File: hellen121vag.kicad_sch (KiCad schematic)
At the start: 122 parts, among them J1 USB_B_Mini, J10 AudioJack_THR, J2 Conn_01x01, J3 Conn_01x01, J4 Conn_01x01, J5 Conn_01x01, J6 Conn_01x01, J7 Conn_01x08, J8 Conn_01x06, M1 Module-can-0.1, M10 Module-can-0.1, M11 Module-vr-0.1, M12 Module-dinput4-0.1, M2 Module-power5-0.2, M3 Module-mcu-0.2, M4 Module-input-0.1, M5 Module-knock-0.1, M6 Module-output-0.2, M7 Module-ign8-0.1, M8 Module-power12-0.2, M9 Module-wbo-0.1, P1 368255-2, P10 Pad, P11 Pad, P12 Pad, P13 Pad, P14 Pad, P17 Pad, P2 Pad, P20 Pad, P28 Pad, P3 Pad, P4 Pad, P40 Pad, P41 Pad, P43 Pad, P44 Pad, P45 Pad, P46 Pad, P48 Pad, P49 Pad, P5 Pad, P56 Pad, P6 Pad, P61 Pad, P63 Pad, P64 Pad, P66 Pad, P67 Pad, P68 Pad, P69 Pad, P7 Pad, P74 Pad, P8 Pad, P80 Pad, P9 Pad, U1 L6205PD, U2 LPS25HB, U3 MCP6002-xSN

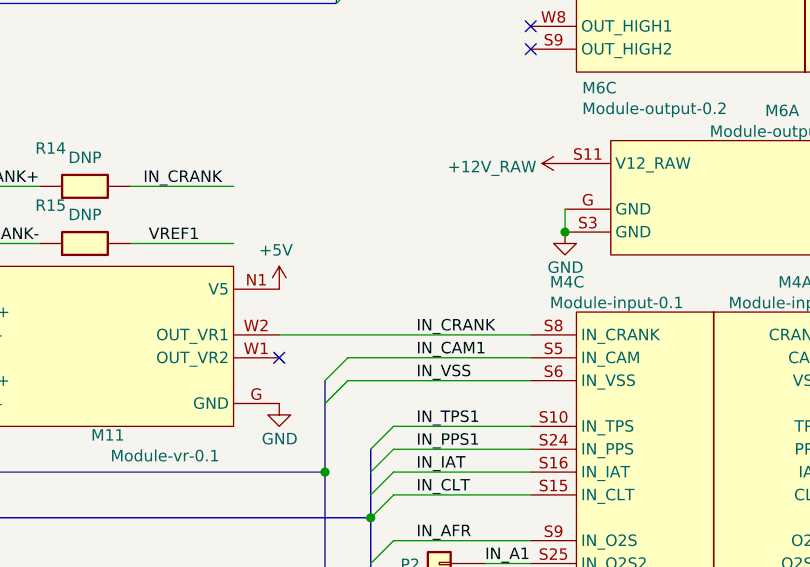
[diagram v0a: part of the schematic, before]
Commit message: Implement & Document trigger HW solder hookup pins #48
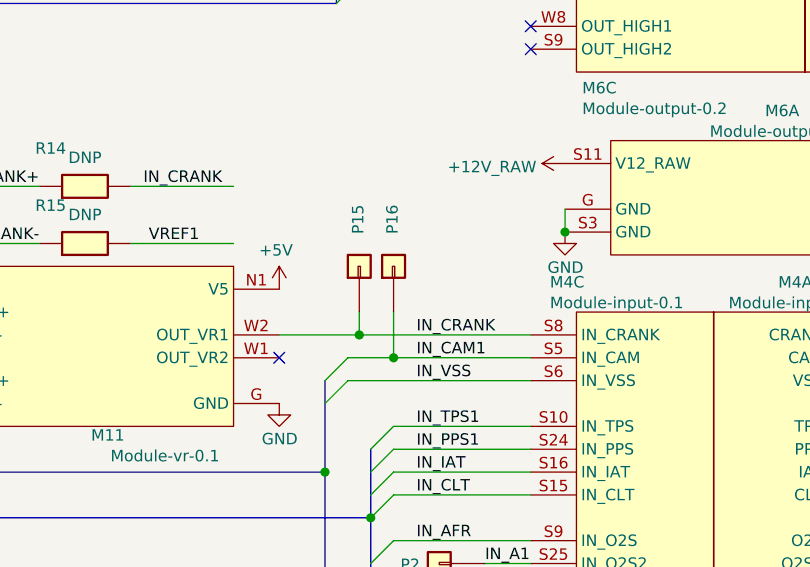
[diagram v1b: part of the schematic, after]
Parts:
- added P15, P16: Pad, hellen-one-common:PAD-TH, symbol hellen-one-common:Pad
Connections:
- net IN_CAM1: now also P16.1 (Pin_1)
- net IN_CRANK: now also P15.1 (Pin_1)
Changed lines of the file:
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@@
-(kicad_sch (version 20210406) (generator eeschema)
+(kicad_sch (version 20210621) (generator eeschema)
   (paper "A2")
   (title_block
@@
   (junction (at 280.67 134.62) (diameter 1.016) (color 0 0 0 0))
   (junction (at 284.48 346.71) (diameter 1.016) (color 0 0 0 0))
+  (junction (at 285.75 196.85) (diameter 1.016) (color 0 0 0 0))
   (junction (at 287.02 119.38) (diameter 1.016) (color 0 0 0 0))
   (junction (at 287.02 121.92) (diameter 1.016) (color 0 0 0 0))
   (junction (at 287.02 273.05) (diameter 1.016) (color 0 0 0 0))
+  (junction (at 289.56 199.39) (diameter 1.016) (color 0 0 0 0))
   (junction (at 294.64 346.71) (diameter 1.016) (color 0 0 0 0))
   (junction (at 302.26 152.4) (diameter 1.016) (color 0 0 0 0))
@@
     (stroke (width 0) (type solid) (color 0 0 0 0))
   )
-  (wire (pts (xy 276.86 196.85) (xy 304.8 196.85))
+  (wire (pts (xy 276.86 196.85) (xy 285.75 196.85))
     (stroke (width 0) (type solid) (color 0 0 0 0))
   )
@@
     (stroke (width 0) (type solid) (color 0 0 0 0))
   )
-  (wire (pts (xy 284.48 199.39) (xy 304.8 199.39))
+  (wire (pts (xy 284.48 199.39) (xy 289.56 199.39))
     (stroke (width 0) (type solid) (color 0 0 0 0))
   )
@@
     (stroke (width 0) (type solid) (color 0 0 0 0))
   )
+  (wire (pts (xy 285.75 194.31) (xy 285.75 196.85))
+    (stroke (width 0) (type solid) (color 0 0 0 0))
+  )
+  (wire (pts (xy 285.75 196.85) (xy 304.8 196.85))
+    (stroke (width 0) (type solid) (color 0 0 0 0))
+  )
   (wire (pts (xy 287.02 119.38) (xy 285.75 119.38))
     (stroke (width 0) (type solid) (color 0 0 0 0))
@@
     (stroke (width 0) (type solid) (color 0 0 0 0))
   )
+  (wire (pts (xy 289.56 194.31) (xy 289.56 199.39))
+    (stroke (width 0) (type solid) (color 0 0 0 0))
+  )
+  (wire (pts (xy 289.56 199.39) (xy 304.8 199.39))
+    (stroke (width 0) (type solid) (color 0 0 0 0))
+  )
   (wire (pts (xy 289.56 207.01) (xy 304.8 207.01))
     (stroke (width 0) (type solid) (color 0 0 0 0))
@@
     (pin "1")
   )
+  (symbol (lib_id "hellen-one-common:Pad") (at 285.75 189.23 90) (unit 1)
+    (in_bom yes) (on_board yes)
+    (property "Reference" "P15" (id 0) (at 285.6144 182.372 0)
+      (effects (font (size 1.27 1.27)) (justify right))
+    )
+    (property "Value" "Pad" (id 1) (at 288.29 189.23 0)
+      (effects (font (size 1.27 1.27)) hide)
+    )
+    (property "Footprint" "hellen-one-common:PAD-TH" (id 2) (at 289.56 189.23 0)
+      (effects (font (size 1.27 1.27)) hide)
+    )
+    (property "Datasheet" "~" (id 3) (at 285.75 189.23 0)
+      (effects (font (size 1.27 1.27)) hide)
+    )
+    (pin "1")
+  )
+  (symbol (lib_id "hellen-one-common:Pad") (at 289.56 189.23 90) (unit 1)
+    (in_bom yes) (on_board yes)
+    (property "Reference" "P16" (id 0) (at 289.4244 182.372 0)
+      (effects (font (size 1.27 1.27)) (justify right))
+    )
+    (property "Value" "Pad" (id 1) (at 292.1 189.23 0)
+      (effects (font (size 1.27 1.27)) hide)
+    )
+    (property "Footprint" "hellen-one-common:PAD-TH" (id 2) (at 293.37 189.23 0)
+      (effects (font (size 1.27 1.27)) hide)
+    )
+    (property "Datasheet" "~" (id 3) (at 289.56 189.23 0)
+      (effects (font (size 1.27 1.27)) hide)
+    )
+    (pin "1")
+  )
   (symbol (lib_id "hellen-one-common:Pad") (at 294.64 222.25 180) (unit 1)
     (in_bom yes) (on_board yes)
@@
       (reference "P14") (unit 1) (value "Pad") (footprint "hellen-one-common:PAD-TH")
     )
+    (path "/631638c1-bba7-416f-b9e2-d63828d88980"
+      (reference "P15") (unit 1) (value "Pad") (footprint "hellen-one-common:PAD-TH")
+    )
+    (path "/6af4d44c-79f6-417d-8cda-630cb6030fe1"
+      (reference "P16") (unit 1) (value "Pad") (footprint "hellen-one-common:PAD-TH")
+    )
     (path "/8149bcf9-72dd-4a61-a70c-152267751b88"

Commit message: less crazy routing for ignition outputs fix #32 Better match injector traces fix #45 Convert to 4 layer fix #56 Connect J1-6 USB cable shield to GND fix #62
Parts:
- added R23: 0, hellen-one-common:R0603, symbol hellen-one-common:Res
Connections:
- net GND: now also R23.2; no longer J1.5 (GND)
- net at J1.6 (Shield): now also J1.5 (GND), R23.1
- no-connect marks 67 -> 66
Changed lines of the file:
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@@
   (junction (at 398.78 382.27) (diameter 1.016) (color 0 0 0 0))
   (junction (at 398.78 397.51) (diameter 1.016) (color 0 0 0 0))
+  (junction (at 478.79 142.24) (diameter 1.016) (color 0 0 0 0))
   (junction (at 505.46 175.26) (diameter 1.016) (color 0 0 0 0))
   (junction (at 511.81 314.96) (diameter 1.016) (color 0 0 0 0))
@@
   (no_connect (at 441.96 170.18))
   (no_connect (at 468.63 149.86))
-  (no_connect (at 478.79 144.78))
   (no_connect (at 535.94 149.86))
   (bus_entry (at 95.25 80.01) (size 2.54 2.54)
@@
     (stroke (width 0) (type solid) (color 0 0 0 0))
   )
+  (wire (pts (xy 476.25 142.24) (xy 476.25 144.78))
+    (stroke (width 0) (type solid) (color 0 0 0 0))
+  )
+  (wire (pts (xy 478.79 142.24) (xy 476.25 142.24))
+    (stroke (width 0) (type solid) (color 0 0 0 0))
+  )
+  (wire (pts (xy 478.79 142.24) (xy 478.79 144.78))
+    (stroke (width 0) (type solid) (color 0 0 0 0))
+  )
   (wire (pts (xy 481.33 193.04) (xy 494.03 193.04))
     (stroke (width 0) (type solid) (color 0 0 0 0))
@@
     (stroke (width 0) (type solid) (color 0 0 0 0))
   )
+  (wire (pts (xy 485.14 142.24) (xy 478.79 142.24))
+    (stroke (width 0) (type solid) (color 0 0 0 0))
+  )
+  (wire (pts (xy 485.14 147.32) (xy 485.14 142.24))
+    (stroke (width 0) (type solid) (color 0 0 0 0))
+  )
   (wire (pts (xy 488.95 205.74) (xy 481.33 205.74))
     (stroke (width 0) (type solid) (color 0 0 0 0))
@@
     (pin "1")
   )
-  (symbol (lib_id "power:GND") (at 476.25 144.78 180) (unit 1)
+  (symbol (lib_id "power:GND") (at 485.14 157.48 0) (unit 1)
     (in_bom yes) (on_board yes)
-    (property "Reference" "#PWR0174" (id 0) (at 476.25 138.43 0)
+    (property "Reference" "#PWR0174" (id 0) (at 485.14 163.83 0)
       (effects (font (size 1.27 1.27)) hide)
     )
-    (property "Value" "GND" (id 1) (at 476.1992 140.8366 0))
-    (property "Footprint" "" (id 2) (at 476.25 144.78 0)
+    (property "Value" "GND" (id 1) (at 485.1908 161.4234 0))
+    (property "Footprint" "" (id 2) (at 485.14 157.48 0)
       (effects (font (size 1.27 1.27)) hide)
     )
-    (property "Datasheet" "" (id 3) (at 476.25 144.78 0)
+    (property "Datasheet" "" (id 3) (at 485.14 157.48 0)
       (effects (font (size 1.27 1.27)) hide)
     )
@@
     (pin "2")
   )
+  (symbol (lib_id "hellen-one-common:Res") (at 485.14 147.32 90) (mirror x) (unit 1)
+    (in_bom yes) (on_board yes)
+    (property "Reference" "R23" (id 0) (at 483.6782 148.832 90))
+    (property "Value" "0" (id 1) (at 482.8002 156.2555 90))
+    (property "Footprint" "hellen-one-common:R0603" (id 2) (at 488.95 151.13 0)
+      (effects (font (size 1.27 1.27)) hide)
+    )
+    (property "Datasheet" "" (id 3) (at 485.14 147.32 0)
+      (effects (font (size 1.27 1.27)) hide)
+    )
+    (property "LCSC" "C23162" (id 4) (at 485.14 147.32 0)
+      (effects (font (size 1.27 1.27)) hide)
+    )
+    (pin "1")
+    (pin "2")
+  )
   (symbol (lib_id "hellen-one-common:Res") (at 524.51 125.73 90) (mirror x) (unit 1)
     (in_bom yes) (on_board yes)
@@
       (reference "R22") (unit 1) (value "10k") (footprint "hellen-one-common:R0603")
     )
+    (path "/a20eb1b0-1b61-4bb7-8cc8-a704d4eedade"
+      (reference "R23") (unit 1) (value "0") (footprint "hellen-one-common:R0603")
+    )
     (path "/9d6f57c0-0eee-4b5b-b98c-463c678c6828"

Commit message: replace VR module with VR-discrete
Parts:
- removed M11: Module-vr-0.1, hellen-one-vr-0.1:vr, symbol hellen-one-vr-0.1:Module-vr-0.1
- removed R14, R15: DNP, hellen-one-common:R1206, symbol hellen-one-common:Res
- added M11: Module-vr-discrete-0.1, hellen-one-vr-discrete-0.1:vr-discrete, symbol vr-discrete:Module-vr-discrete-0.1
- M3: value Module-mcu-0.2 -> Module-mcu-0.5
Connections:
- net +5V: now also M11.E4 (V5_IN)
- net FUEL_CONSUM: now also M3.E18 (OUT_PWM6), M11.E1 (Thresh_IN)
- net GND: now also M11.G (GND)
- net IDLE: no longer M3.E18 (OUT_PWM6)
- net IN_CRANK: now also M11.E3 (OUT)
- net IN_CRANK+: now also M11.W2 (VR+)
- net IN_CRANK-: now also M11.W1 (VR-)
- net VR_ANALOG: now reaches M3.S8 (IN_SENS1)
- net VR_ANALOG: now also M11.E2 (OUT_A)
- no-connect marks 66 -> 62

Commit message: DRC warnings. Silk under module under copper. VVT diode.
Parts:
- D10, D11, D12: value 1N4148WS -> B5819W; footprint hellen-one-common:SOD-323 -> Diode_SMD:D_SOD-123
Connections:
- net FUEL_CONSUM: no longer M11.E1 (Thresh_IN), M3.E18 (OUT_PWM6)
- net IDLE: now also M3.E23 (OUT_IO4)
- new net THRESHOLD_VR: M11.E1 (Thresh_IN), M3.E18 (OUT_PWM6)
- no-connect marks 62 -> 61
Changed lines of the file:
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@@
   (no_connect (at 400.05 265.43))
   (no_connect (at 400.05 267.97))
-  (no_connect (at 401.32 142.24))
   (no_connect (at 401.32 154.94))
   (no_connect (at 401.32 160.02))
@@
     (stroke (width 0) (type solid) (color 0 0 0 0))
   )
-  (wire (pts (xy 383.54 127) (xy 383.54 172.974))
+  (wire (pts (xy 383.54 124.46) (xy 383.54 172.974))
     (stroke (width 0) (type solid) (color 0 0 0 0))
   )
-  (wire (pts (xy 383.54 127) (xy 401.32 127))
+  (wire (pts (xy 383.54 124.46) (xy 401.32 124.46))
     (stroke (width 0) (type solid) (color 0 0 0 0))
   )
@@
     (stroke (width 0) (type solid) (color 0 0 0 0))
   )
-  (wire (pts (xy 387.35 124.46) (xy 401.32 124.46))
+  (wire (pts (xy 387.35 127) (xy 401.32 127))
+    (stroke (width 0) (type solid) (color 0 0 0 0))
+  )
+  (wire (pts (xy 387.35 142.24) (xy 401.32 142.24))
     (stroke (width 0) (type solid) (color 0 0 0 0))
   )
@@
     (effects (font (size 1.27 1.27)) (justify left bottom))
   )
-  (label "FUEL_CONSUM" (at 361.95 109.22 0)
-    (effects (font (size 1.27 1.27)) (justify left bottom))
-  )
   (label "IN_VIGN" (at 363.22 382.27 0)
     (effects (font (size 1.27 1.27)) (justify left bottom))
   )
-  (label "IDLE" (at 364.744 125.222 0)
+  (label "FUEL_CONSUM" (at 369.57 109.22 0)
     (effects (font (size 1.27 1.27)) (justify left bottom))
   )
@@
     (effects (font (size 1.27 1.27)) (justify left bottom))
   )
-  (label "THRESHOLD_VR" (at 387.35 124.46 0)
+  (label "FUEL_CONSUM" (at 387.35 127 0)
+    (effects (font (size 1.27 1.27)) (justify left bottom))
+  )
+  (label "IDLE" (at 387.35 142.24 0)
     (effects (font (size 1.27 1.27)) (justify left bottom))
   )
@@
     (effects (font (size 1.27 1.27)) (justify left bottom))
   )
-  (label "FUEL_CONSUM" (at 388.62 127 0)
-    (effects (font (size 1.27 1.27)) (justify left bottom))
-  )
   (label "WASTEGATE" (at 388.62 137.16 0)
     (effects (font (size 1.27 1.27)) (justify left bottom))
@@
     (in_bom yes) (on_board yes)
     (property "Reference" "D10" (id 0) (at 274.32 118.9798 0))
-    (property "Value" "1N4148WS" (id 1) (at 274.32 122.5485 0))
-    (property "Footprint" "hellen-one-common:SOD-323" (id 2) (at 266.7 114.3 0)
+    (property "Value" "B5819W" (id 1) (at 274.32 122.5485 0))
+    (property "Footprint" "Diode_SMD:D_SOD-123" (id 2) (at 266.7 114.3 0)
       (effects (font (size 1.27 1.27)) hide)
     )
@@
     (in_bom yes) (on_board yes)
     (property "Reference" "D11" (id 0) (at 274.32 124.0598 0))
-    (property "Value" "1N4148WS" (id 1) (at 274.32 127.6285 0))
-    (property "Footprint" "hellen-one-common:SOD-323" (id 2) (at 266.7 119.38 0)
+    (property "Value" "B5819W" (id 1) (at 274.32 127.6285 0))
+    (property "Footprint" "Diode_SMD:D_SOD-123" (id 2) (at 266.7 119.38 0)
       (effects (font (size 1.27 1.27)) hide)
     )
@@
     (in_bom yes) (on_board yes)
     (property "Reference" "D12" (id 0) (at 274.32 129.1398 0))
-    (property "Value" "1N4148WS" (id 1) (at 274.32 132.7085 0))
-    (property "Footprint" "hellen-one-common:SOD-323" (id 2) (at 266.7 124.46 0)
+    (property "Value" "B5819W" (id 1) (at 274.32 132.7085 0))
+    (property "Footprint" "Diode_SMD:D_SOD-123" (id 2) (at 266.7 124.46 0)
       (effects (font (size 1.27 1.27)) hide)
     )
@@
     )
     (path "/2a7e2237-4297-404c-bd4f-329b18c9a4c7"
-      (reference "D10") (unit 1) (value "1N4148WS") (footprint "hellen-one-common:SOD-323")
+      (reference "D10") (unit 1) (value "B5819W") (footprint "Diode_SMD:D_SOD-123")
     )
     (path "/43f96b0c-8c9b-45d4-a297-7c84dbefbe78"
-      (reference "D11") (unit 1) (value "1N4148WS") (footprint "hellen-one-common:SOD-323")
+      (reference "D11") (unit 1) (value "B5819W") (footprint "Diode_SMD:D_SOD-123")
     )
     (path "/742fdbb1-e8c7-4f9e-bfa8-b46105674196"
-      (reference "D12") (unit 1) (value "1N4148WS") (footprint "hellen-one-common:SOD-323")
+      (reference "D12") (unit 1) (value "B5819W") (footprint "Diode_SMD:D_SOD-123")
     )
     (path "/779a20b8-3f8c-45a0-b2d9-ad950cd71a9a"

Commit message: rev. c fab time?
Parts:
- removed M9: Module-wbo-0.1, hellen-one-wbo-0.1:wbo, symbol hellen-one-wbo-0.1:Module-wbo-0.1
- added D13, D14: B5819W, Diode_SMD:D_SOD-123, symbol hellen-one-common:1N4148WS
- added M9: Module-wbo-0.3, hellen-one-wbo-0.3:wbo, symbol hellen-one-wbo-0.3:Module-wbo-0.3
- D10, D11, D12: LCSC C2128 -> C8598
- R23: LCSC C23162 -> C21189
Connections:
- net +12V_RAW: now also D13.1 (K), D14.1 (K)
- net +5V: now also M9.W1 (V5_IN)
- net GND: now also M9.E6 (LSU_H-), M9.G (GND)
- net LSU_CALIBR_RES: now also M9.E4 (LSU_Rtrim)
- net LSU_HEAT-: now also M9.E5 (LSU_H+)
- net LSU_PUMP_I: now also M9.E3 (LSU_Ip)
- net LSU_SENSOR_U: now also M9.E1 (LSU_Un)
- net LSU_SENSOR_U/PUMP_I: now also M9.E2 (LSU_Vm)
- net OUT_VVT1_1: now also D14.2 (A)
- net OUT_VVT1_2: now also D13.2 (A)
- net at M10.V2 (CAN_VIO): now also M9.W2 (CAN_VIO)
- net at M10.V6 (CAN_RX): now also M9.W3 (CAN_RX)
- net at M10.V5 (CAN_TX): now also M9.W4 (CAN_TX)
- net at J8.5 (Pin_5): now also M9.W5 (nReset)
- net at J8.4 (Pin_4): now also M9.W6 (SWDIO)
- net at J8.2 (Pin_2): now also M9.W7 (SWCLK)
- net at J8.1 (Pin_1): now also M9.W8 (V33_OUT)
- net IN_KNOCK2: no longer names the net of M4.S3 (IN_SENS3)
- net IN_KNOCK2_RAW: no longer names the net of P1.107
- net IO1: no longer names the net of M3.N12 (IO1)
- net IO2: no longer names the net of M3.N13 (IO2)
- net IO3: no longer names the net of M3.N14 (IO3)
- net IO4: no longer names the net of M3.N15 (IO4)
- net KNOCK2: no longer names the net of M4.N24 (SENS3)
- new net: M9.J2 (SEL2), M9.J_VCC2 (PULL_UP2)
- no-connect marks 61 -> 72
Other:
- note added: "#1"
- note added: "TODO: knock 2"
- moved on the sheet: BT1, C1, C10, C11, C12, C13, C14, C15, C16, C17, C2, C3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

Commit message: Upd PCB
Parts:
- removed M12: Module-dinput4-0.1, hellen-one-dinput4-0.1:dinput4, symbol hellen-one-dinput4-0.1:Module-dinput4-0.1
- removed M2: Module-power5-0.2, hellen-one-power5-0.1:power5, symbol hellen-one-power5-0.1:Module-power5-0.1
- removed M3: Module-mcu-0.5, hellen-one-mcu-0.2:mcu, symbol hellen-one-mcu-0.2:Module-mcu-0.2
- removed M6: Module-output-0.2, hellen-one-output-0.2:output, symbol hellen-one-output-0.2:Module-output-0.2
- removed M7: Module-ign8-0.1, hellen-one-ign8-0.1:ign8, symbol hellen-one-ign8-0.1:Module-ign8-0.1
- added C18, C19: 1u, hellen-one-common:C0603, symbol hellen-one-common:Cap
- added M2: Module-power5-0.2, hellen-one-power5-0.2:power5, symbol hellen-one-power5-0.2:Module-power5-0.2
- added M3: Module-mcu-0.7, hellen-one-mcu-0.7:mcu, symbol hellen-one-mcu-0.7:Module-mcu-0.7
- added M6: Module-output-0.3, hellen-one-output-0.3:output, symbol hellen-one-output-0.3:Module-output-0.3
- added M7: Module-ign8-0.2, hellen-one-ign8-0.2:ign8, symbol hellen-one-ign8-0.2:Module-ign8-0.2
- added U4: TLS115_SOIC, kicad6-libraries:PG-DSO-8-43_VIA, symbol hellen-one-common:TLS115
- added U5: TLS115_SON, Package_SON:HVSON-8-1EP_3x3mm_P0.65mm_EP1.6x2.4mm, symbol hellen-one-common:TLS115
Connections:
- net +12V: now also M2.V1 (V12)
- net +12V_PROT: now also C18.2, M6.W5 (V12P), U4.7 (EN), U4.8 (IN), U5.7 (EN), U5.8 (IN)
- net +12V_RAW: now also M6.S11 (V12_RAW)
- net +3V3: now also M3.N16 (V33)
- net +5V: now also M2.V2 (V5), M3.S1 (V5), M6.W14 (V5), U4.5 (ADJ), U5.5 (ADJ)
- net +5VA: now also M3.S33 (V5A); no longer P1.53, P1.72, P1.73, P1.83, P1.98
- net +ETB: now also M3.E14 (OUT_PWM2)
- net -ETB: now also M3.E15 (OUT_PWM3)
- net A1: now also M3.S30 (IN_O2S2)
- net A2: now also M3.S22 (IN_MAP3)
- net A3: now also M3.S26 (IN_AUX3)
- net A4: now also M3.S23 (IN_DIG3)
- net AFR: now also M3.S16 (IN_O2S)
- net BOOT0: now also M3.N28 (BOOT0)
- net CAM1: now also M3.S15 (IN_AN_DIG2)
- net CAM2: now also M3.S27 (IN_AUX4)
- net CAN_RX: now also M3.N2 (CAN_RX)
- net CAN_TX: now also M3.N3 (CAN_TX)
- net CAN_VIO: now also M3.N1 (CAN_VIO)
- net CHECK_ENGINE: now also M3.E22 (OUT_IO8), M6.W25 (LOW6_DIODE)
- net CLT: now also M3.S18 (IN_CLT)
- net CRANK: now also M3.S13 (IN_AN_DIG1)
- net D1: now also M4.N26 (SENS1), M3.S3 (IN_DIG8)
- net D2: now also M4.N25 (SENS2), M3.S4 (IN_DIG9)
- net D3: now also M4.N24 (SENS3), M3.S5 (IN_DIG10)
- net D4: now also M4.N23 (SENS4), M3.S6 (IN_DIG11)
- net ETB_EN: now also M3.E13 (OUT_IO12)
- net FUEL_CONSUM: now also M3.E19 (OUT_PWM7), M6.W22 (PP2)
- net FUEL_PUMP_RELAY: now also M3.E8 (OUT_IO1), M6.W35 (LOW11)
- net GND: now also C18.1, C19.1, M2.G (GND), M3.S2 (GND), M6.G (GND), M6.S3 (GND), M7.G (GND), U4.3 (GND), U4.9 (GND), U5.3 (GND), U5.9 (GND)
- net GNDA: now also M4.J23 (PULL_SENS4), M4.J25 (PULL_SENS2), M4.J26 (PULL_SENS1), M3.S32 (GNDA)
- net IAT: now also M3.S19 (IN_IAT)
- net IDLE: now also M3.E23 (OUT_IO4), M6.W38 (LOW3_DUAL)
- net IGN1: now also M3.W1 (OUT_IGN1), M7.V8 (IGN1)
- net IGN2: now also M3.W2 (OUT_IGN2), M7.V7 (IGN2)
- net IGN3: now also M3.W3 (OUT_IGN3), M7.V6 (IGN3)
- net IGN4: now also M3.W4 (OUT_IGN4), M7.V5 (IGN4)
- net IGN5: now also M3.W5 (OUT_IGN5), M7.V4 (IGN5)
- net IGN6: now also M3.W6 (OUT_IGN6), M7.V3 (IGN6)
- net IGN7: now also M3.W7 (OUT_IGN7), M7.V2 (IGN7)
- net IGN8: now also M3.W8 (OUT_IGN8), M7.V1 (IGN8)
- net IGN_V33: now also M3.W10 (IGN_V33), M7.V10 (V33)
- net IGN_V5: now also M3.W9 (IGN_V5), M7.V9 (VCC)
- net INJ1: now also M3.E25 (OUT_INJ1), M6.W24 (INJ1)
- net INJ2: now also M3.E26 (OUT_INJ2), M6.W23 (INJ2)
- net INJ3: now also M3.E29 (OUT_INJ3), M6.W20 (INJ3)
- net INJ4: now also M3.E30 (OUT_INJ4), M6.W19 (INJ4)
- net INJ5: now also M3.E31 (OUT_INJ5), M6.W18 (INJ5)
- net INJ6: now also M3.E32 (OUT_INJ6), M6.W17 (INJ6)
- net INJ7: now also M3.E33 (OUT_INJ7), M6.W16 (INJ7)
- net INJ8: now also M3.E34 (OUT_INJ8), M6.W15 (INJ8)
- net IN_D1: now also M4.S1 (IN_SENS1)
- net IN_D2: now also M4.S2 (IN_SENS2)
- net IN_D3: now also M4.S3 (IN_SENS3)
- net IN_D4: now also M4.S4 (IN_SENS4)
- net KNOCK1: now also M3.S12 (IN_KNOCK)
- net MAF: now also M3.S20 (IN_MAP1)
- net MAIN_RELAY: now also M3.E6 (OUT_IO3), M6.W40 (LOW5_MAIN)
- net MAP2: now also M3.S21 (IN_MAP2)
- net NRESET: now also M3.N24 (nReset)
- net OUT1: now also M3.E7 (OUT_IO5), M6.W39 (LOW7_HIGH1)
- net OUT2: now also M3.E9 (OUT_IO6), M6.W37 (LOW8_HIGH2)
- net OUT3: now also M3.E28 (OUT_PWM8), M6.W21 (LOW1)
- net OUT_CHECK_ENGINE: now also M6.W3 (OUT_LOW6_DIODE)
- net OUT_FUEL_CONSUM: now also M6.S6 (OUT_PP2)
- net OUT_FUEL_PUMP_RELAY: now also M6.S10 (OUT_LOW11)
- net OUT_IDLE: now also M6.S7 (OUT_LOW3_DUAL)
- net OUT_IGN1: now also M7.S8 (OUT_IGN1)
- net OUT_IGN2: now also M7.S7 (OUT_IGN2)
- net OUT_IGN3: now also M7.S6 (OUT_IGN3)
- net OUT_IGN4: now also M7.S5 (OUT_IGN4)
- net OUT_IGN5: now also M7.S4 (OUT_IGN5)
- net OUT_IGN6: now also M7.S3 (OUT_IGN6)
- net OUT_IGN7: now also M7.S2 (OUT_IGN7)
- net OUT_IGN8: now also M7.S1 (OUT_IGN8)
- net OUT_INJ1: now also M6.S18 (OUT_INJ1)
- net OUT_INJ2: now also M6.S16 (OUT_INJ2)
- net OUT_INJ3: now also M6.S17 (OUT_INJ3)
- net OUT_INJ4: now also M6.W7 (OUT_INJ4)
- net OUT_INJ5: now also M6.W10 (OUT_INJ5)
- net OUT_INJ6: now also M6.S15 (OUT_INJ6)
- net OUT_INJ7: now also M6.W12 (OUT_INJ7)
- net OUT_INJ8: now also M6.W11 (OUT_INJ8)
- net OUT_MAIN_RELAY: now also M6.W13 (OUT_LOW5_MAIN)
- net OUT_TACH: now also M6.W6 (OUT_PP1)
- net OUT_VVT1_1: now also M6.S13 (OUT_LOW12), M6.S14 (OUT_LOW9)
- net OUT_VVT1_2: now also M6.W1 (OUT_LOW2), M6.W2 (OUT_LOW10)
- net OUT_VVT2_B1: now also M6.S5 (OUT_SOLENOID_B2)
- net OUT_VVT2_B2: now also M6.S4 (OUT_SOLENOID_B1)
- net OUT_WASTEGATE: now also M6.W4 (OUT_LOW4_DUAL)
- net PPS1: now also M3.S29 (IN_PPS)
- net PPS2: now also M3.S25 (IN_AUX2)
- net RES1: now also M3.S28 (IN_DIG1)
- net RES2: now also M3.S31 (IN_DIG2)
- net RX1: now also M3.N5 (UART8_RX)
- net RX2: now also M3.N7 (UART2_RX)
- net SPI3_CS: now also M3.N8 (SPI3_CS)
- net SPI3_MISO: now also M3.N10 (SPI3_MISO)
- net SPI3_MOSI: now also M3.N11 (SPI3_MOSI)
- net SPI3_SCK: now also M3.N9 (SPI3_SCK)
- net TACH: now also M3.E27 (OUT_PWM1), M6.W28 (PP1)
- net THRESHOLD_VR: now also M3.E18 (OUT_PWM6)
- net TPS1: now also M3.S17 (IN_TPS)
- net TPS2: now also M3.S24 (IN_AUX1)
- net TX1: now also M3.N4 (UART8_TX)
- net TX2: now also M3.N6 (UART2_TX)
- net USBM: now also M3.N31 (USB1M)
- net USBP: now also M3.N30 (USB1P)
- net VBAT: now also M3.N17 (VBAT)
- net VBUS: now also M3.N29 (VBUS)
- net VIGN: now also M3.S7 (VIGN)
- net VR_ANALOG: now also M3.S8 (IN_DIG4)
- net VSS: now also M3.S14 (IN_AN_DIG3)
- net VVT1_1: now also M3.E10 (OUT_IO10), M6.W27 (LOW9), M6.W36 (LOW12)
- net VVT1_2: now also M3.E21 (OUT_IO7), M6.W26 (LOW10), M6.W29 (LOW2)
- net VVT2_B1: now also M3.E17 (OUT_PWM5), M6.W30 (SOLENOID_B2)
- net VVT2_B2: now also M3.E16 (OUT_PWM4), M6.W31 (SOLENOID_B1)
- net WASTEGATE: now also M3.E12 (OUT_IO2), M6.W34 (LOW4_DUAL)
- net at P7.1 (Pin_1): now also M6.W9 (OUT_LOW7_PULLUP)
- net at R19.2, U2.4 (SDA/MOSI): now also M3.N18 (I2C_SDA)
- net at R18.2, U2.2 (SCL/SCLK): now also M3.N19 (I2C_SCL)
- net at P8.1 (Pin_1): now also M6.S12 (OUT_LOW8_PULLUP)
- net at P6.1 (Pin_1): now also M6.S8 (OUT_LOW1)
- new net +5VP: C19.2, P1.53, P1.72, P1.73, P1.83, P1.98, U4.1 (OUT), U5.1 (OUT)
- no-connect marks 72 -> 62
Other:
- note added: "C540240"
- note added: "C540241"
- note added: "C540242"
- note added: "C540243"
- note added: "Protected 5V analog power supply"
- note added: "SOIC-8"
- note added: "TSON-10"
